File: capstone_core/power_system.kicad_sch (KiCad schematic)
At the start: 0 parts

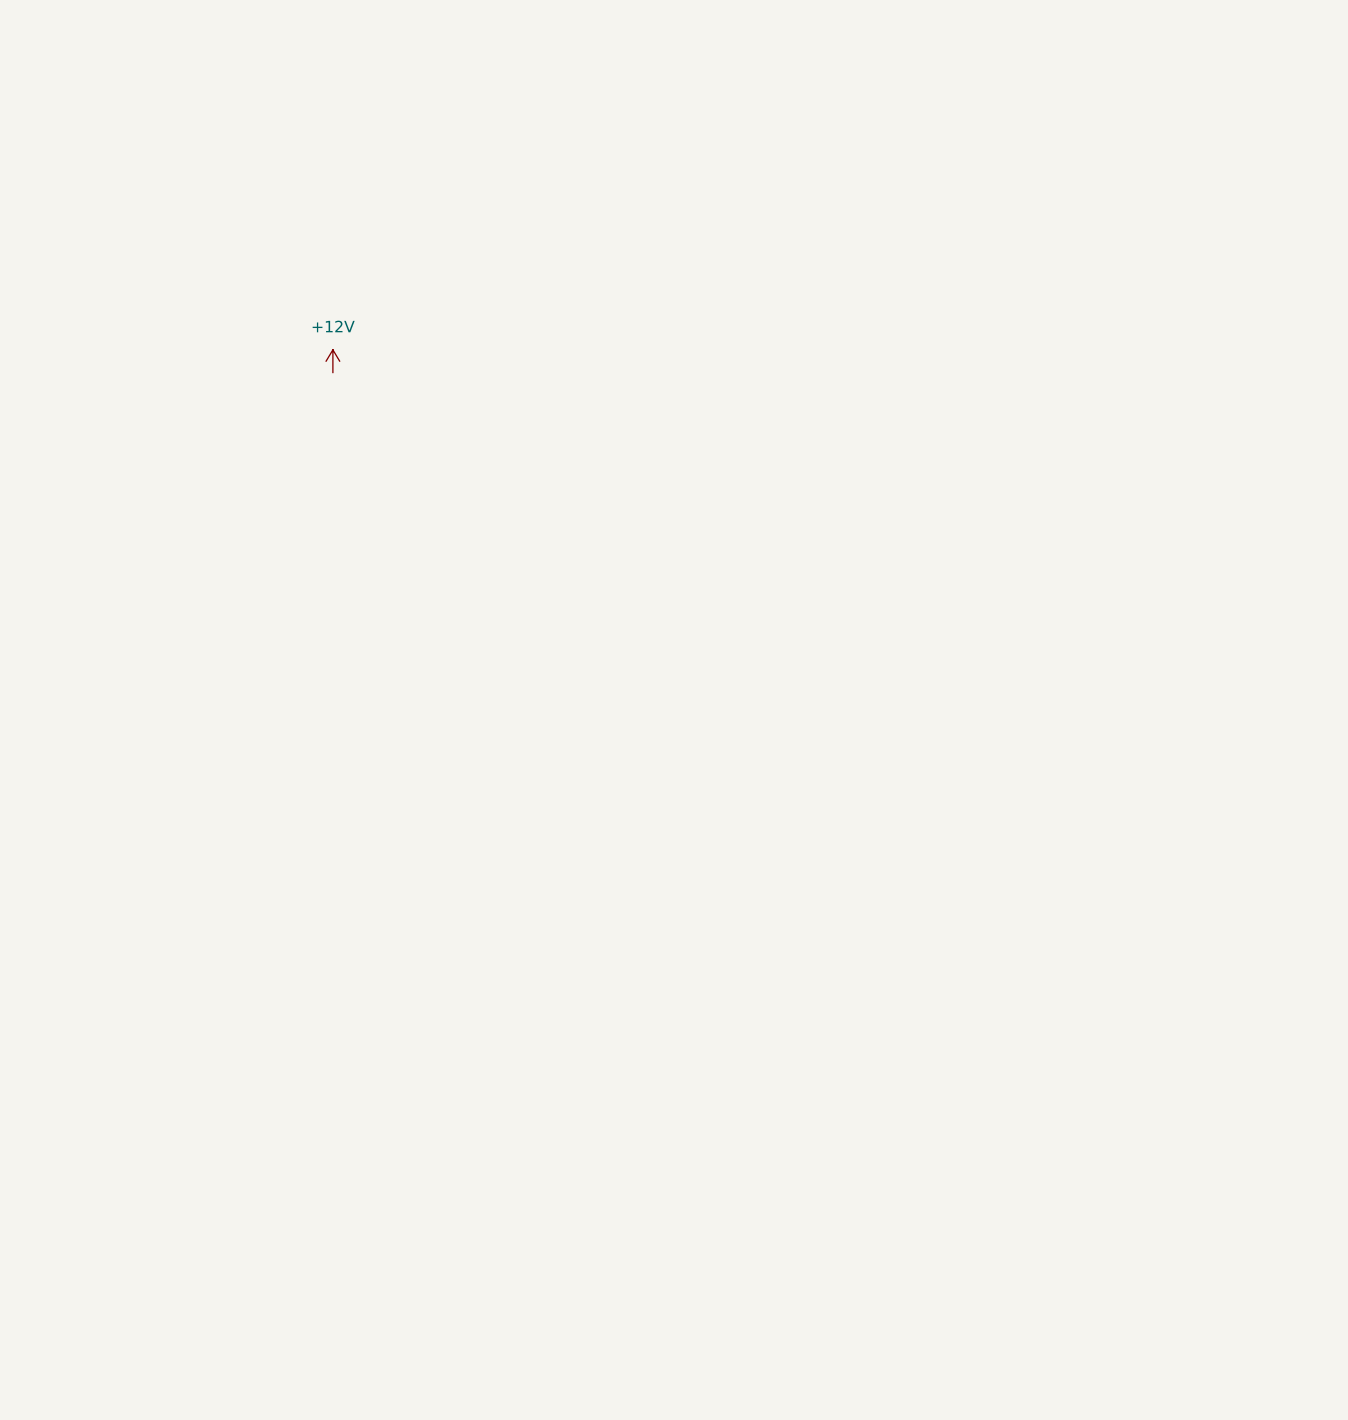
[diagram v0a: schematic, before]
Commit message: adding connectors, components, and footprints
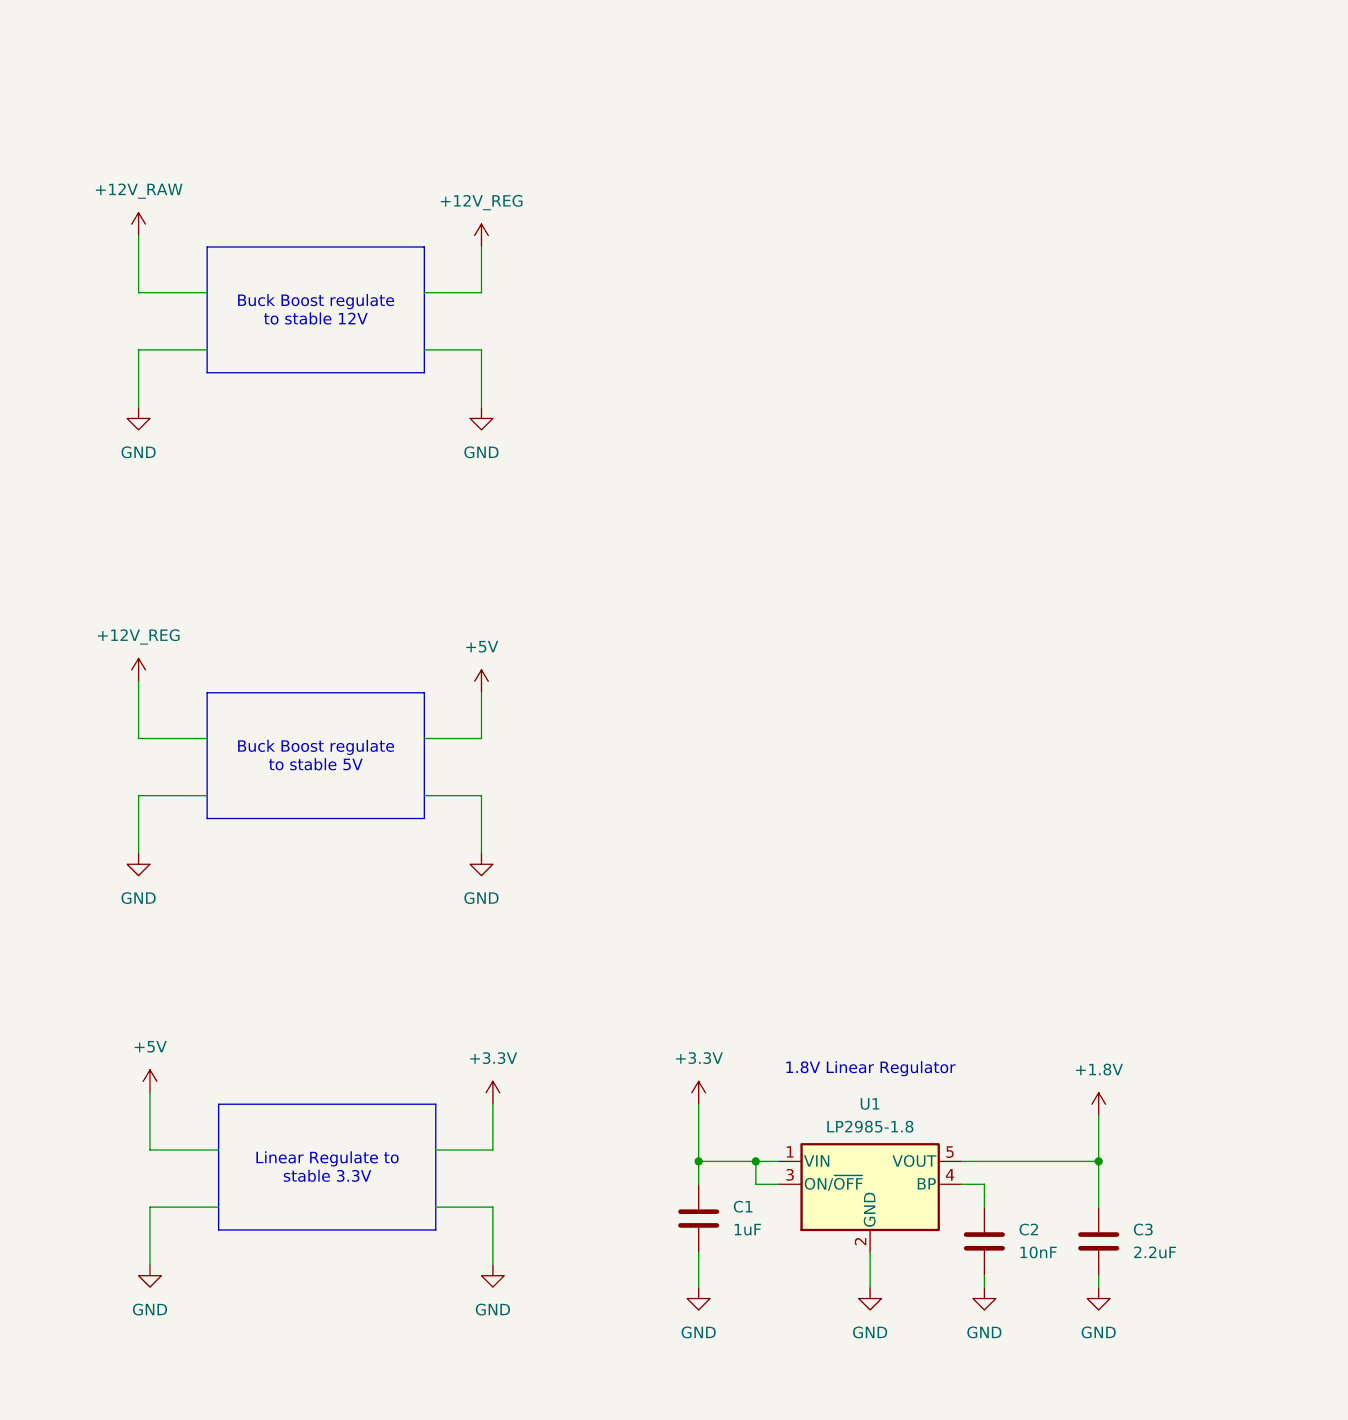
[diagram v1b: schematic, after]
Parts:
- added C1: 1uF, symbol Device:C
- added C2: 10nF, symbol Device:C
- added C3: 2.2uF, symbol Device:C
- added U1: LP2985-1.8, symbol Regulator_Linear:LP2985-1.8
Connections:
- new net: C2.1, U1.4 (BP)
- new net +1.8V: C3.1, U1.5 (VOUT)
- new net +3.3V: C1.1, U1.1 (VIN), U1.3 (ON/~{OFF})
- new net GND: C1.2, C2.2, C3.2, U1.2 (GND)
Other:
- note added: "1.8V Linear Regulator"

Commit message: Update Power System .kicad_sch
Added 3.3V linear regulator, buck boost circuits to stable 12V and drop to 5V
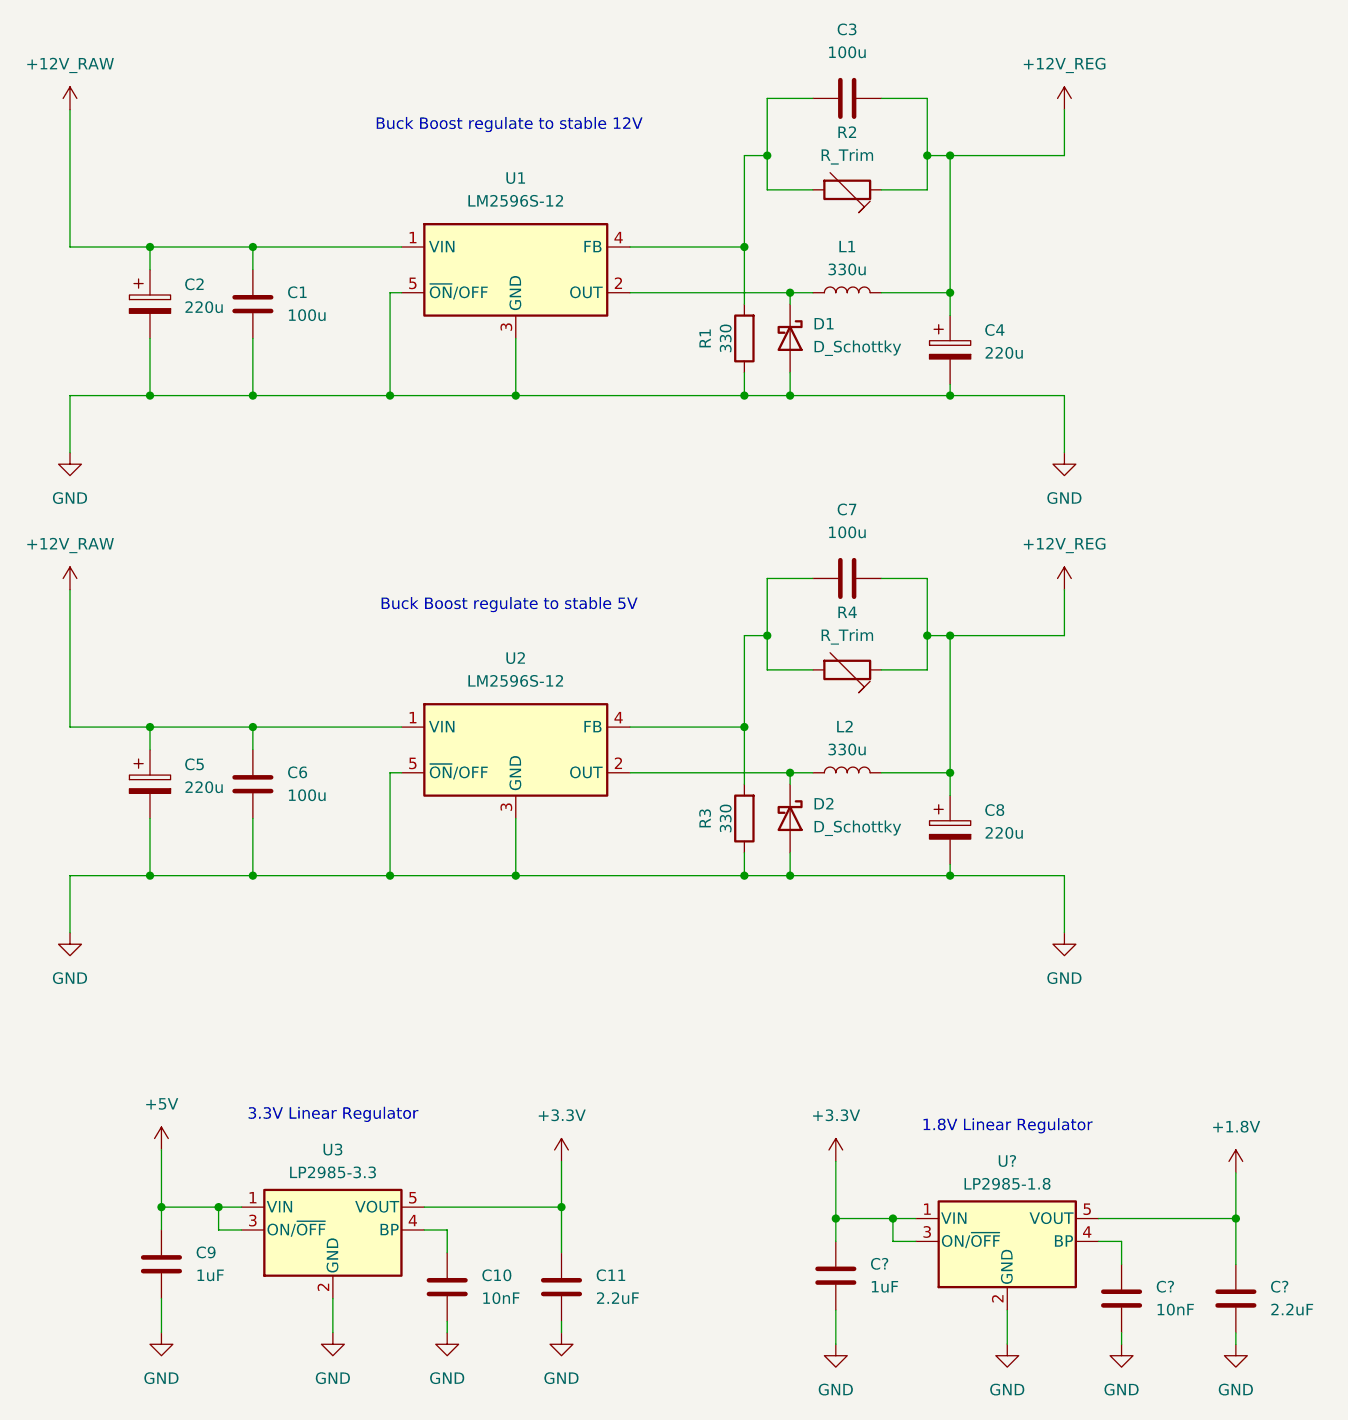
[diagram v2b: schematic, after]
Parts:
- added C1, C3, C6, C7: 100u, symbol Device:C
- added C10: 10nF, symbol Device:C
- added C11: 2.2uF, symbol Device:C
- added C2, C4, C5, C8: 220u, symbol Device:C_Polarized
- added C9: 1uF, symbol Device:C
- added D1, D2: D_Schottky, symbol Device:D_Schottky
- added L1, L2: 330u, symbol Device:L
- added R1, R3: 330, symbol Device:R
- added R2, R4: R_Trim, symbol Device:R_Trim
- added U1, U2: LM2596S-12, Package_TO_SOT_SMD:TO-263-5_TabPin3, symbol Regulator_Switching:LM2596S-12
- added U3: LP2985-3.3, Package_TO_SOT_SMD:SOT-23-5, symbol Regulator_Linear:LP2985-3.3
- renumbered C1 to C?, C3 to C?, C2 to C?, U1 to U?
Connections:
- net +12V_RAW: now also C1.1, C2.1, C5.1, C6.1, U1.1 (VIN), U2.1 (VIN)
- net +12V_REG: now also C3.2, C4.1, C7.2, C8.1, L1.2, L2.2, R2.1, R4.1
- net +3.3V: now also C11.1, U3.5 (VOUT)
- net +5V: now also C9.1, U3.1 (VIN), U3.3 (ON/~{OFF})
- net GND: now also C1.2, C10.2, C11.2, C2.2, C4.2, C5.2, C6.2, C8.2, C9.2, D1.2 (A), D2.2 (A), R1.1, R3.1, U1.3 (GND), U1.5 (~{ON}/OFF), U2.3 (GND), U2.5 (~{ON}/OFF), U3.2 (GND)
- new net: D2.1 (K), L2.1, U2.2 (OUT)
- new net: C3.1, R1.2, R2.2, U1.4 (FB)
- new net: C10.1, U3.4 (BP)
- new net: D1.1 (K), L1.1, U1.2 (OUT)
- new net: C7.1, R3.2, R4.2, U2.4 (FB)
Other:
- note added: "3.3V Linear Regulator"
- note added: "Buck Boost regulate to stable 12V"
- note added: "Buck Boost regulate to stable 5V"
- moved on the sheet: C?, U?
